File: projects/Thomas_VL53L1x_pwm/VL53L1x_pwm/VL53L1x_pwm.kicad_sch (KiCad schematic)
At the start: 26 parts, among them J1 Conn_02x05_Odd_Even, J2 Conn_01x04, Q1 BSS138, Q2 BSS138, Q3 BSS138, Q4 BSS138, U1 LP2985-1.8, U2 STM32L011D4Px, U3 VL53L1CXV0FY1, Y1 16 MHz 9 pF

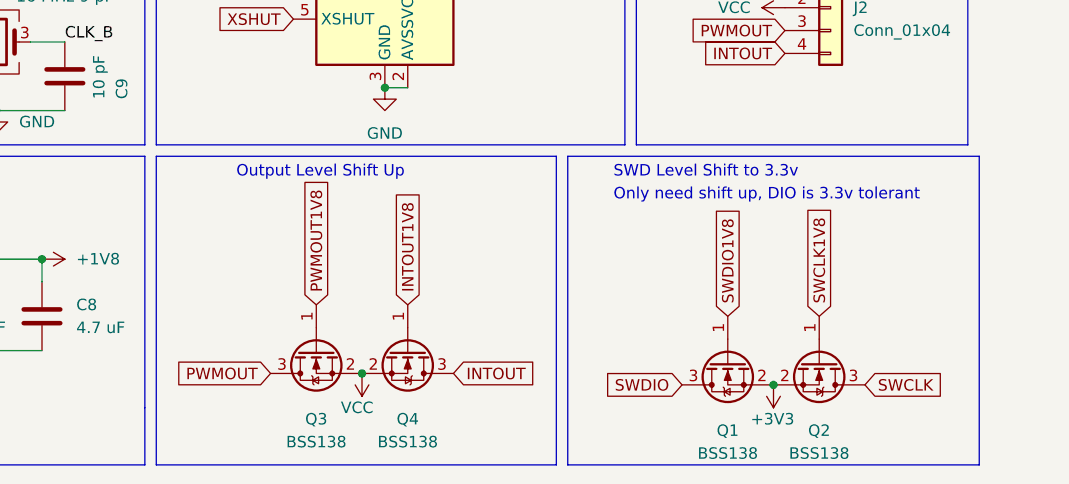
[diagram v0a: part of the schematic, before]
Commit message: Fix really stupid hardware bug Lesson learned: check spice BEFORE committing
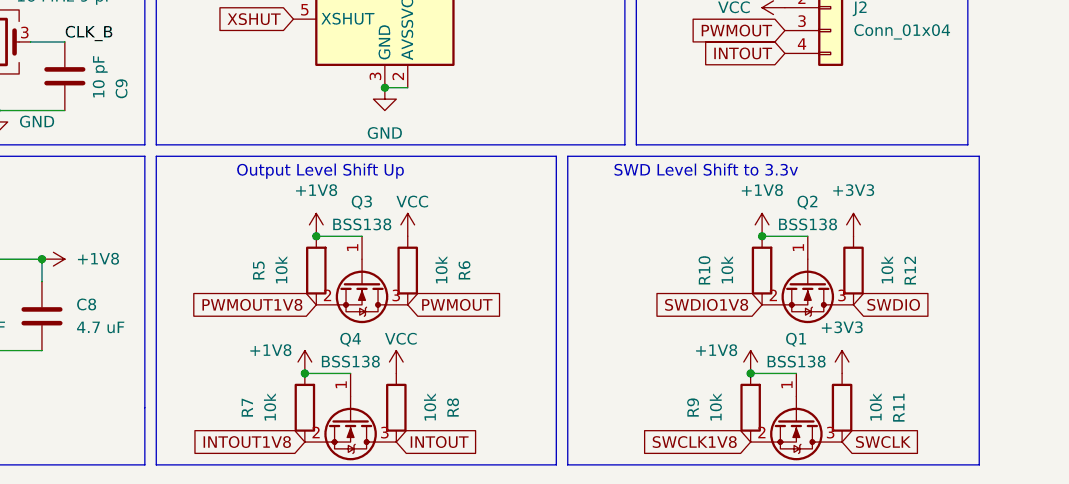
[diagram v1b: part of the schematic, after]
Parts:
- added R10, R11, R12, R5, R6, R7, R8, R9: 10k, Resistor_SMD:R_0402_1005Metric, symbol Device:R
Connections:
- net +1V8: now also Q1.1 (G), Q2.1 (G), Q3.1 (G), Q4.1 (G), R10.2, R5.2, R7.2, R9.2
- net +3V3: now also R11.1, R12.1; no longer Q1.2 (S), Q2.2 (S)
- net INTOUT: now also R8.2
- net INTOUT1V8: now also Q4.2 (S), R7.1; no longer Q4.1 (G)
- net PWMOUT: now also R6.2
- net PWMOUT1V8: now also Q3.2 (S), R5.1; no longer Q3.1 (G)
- net SWCLK: now also Q1.3 (D), R11.2; no longer Q2.3 (D)
- net SWCLK1V8: now also Q1.2 (S), R9.1; no longer Q2.1 (G)
- net SWDIO: now also Q2.3 (D), R12.2; no longer Q1.3 (D)
- net SWDIO1V8: now also Q2.2 (S), R10.1; no longer Q1.1 (G)
- net VCC: now also R6.1, R8.1; no longer Q3.2 (S), Q4.2 (S)
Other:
- note removed: "Only need shift up, DIO is 3.3v tolerant"
- moved on the sheet: Q3, Q4
